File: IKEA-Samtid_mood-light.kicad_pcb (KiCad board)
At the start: 2 copper layers, 100 x 100 mm, 156 parts, among them IC1 ATMEGA168PA-M, P1 FTDI, P2 POWER, P3.1 B-to-B-1A, P3.2 B-to-B-1B, P4.1 B-to-B-2A, P4.2 B-to-B-2B, Q1 BSS138, Q2 BSS138, SW1 ENTER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

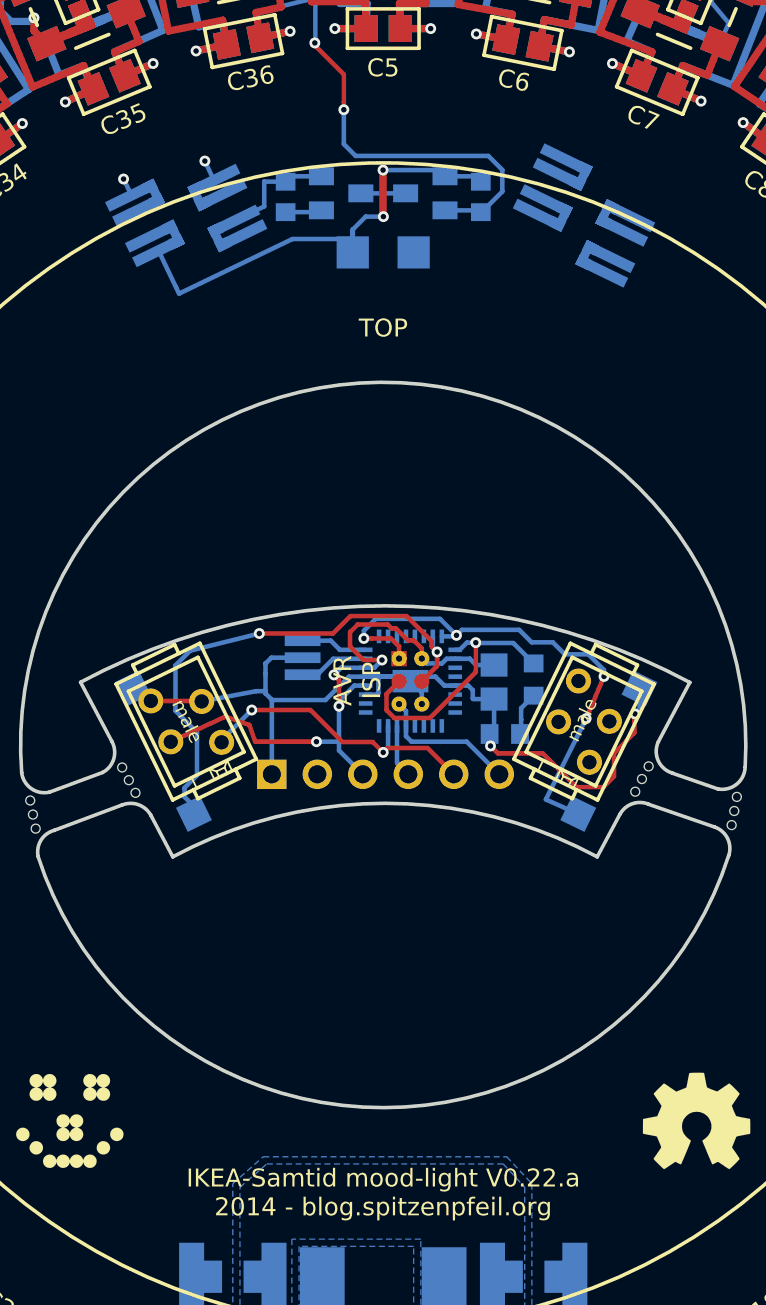
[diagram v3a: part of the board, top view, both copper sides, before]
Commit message: Had the pull-up voltages reversed on the MOSFET isolator.
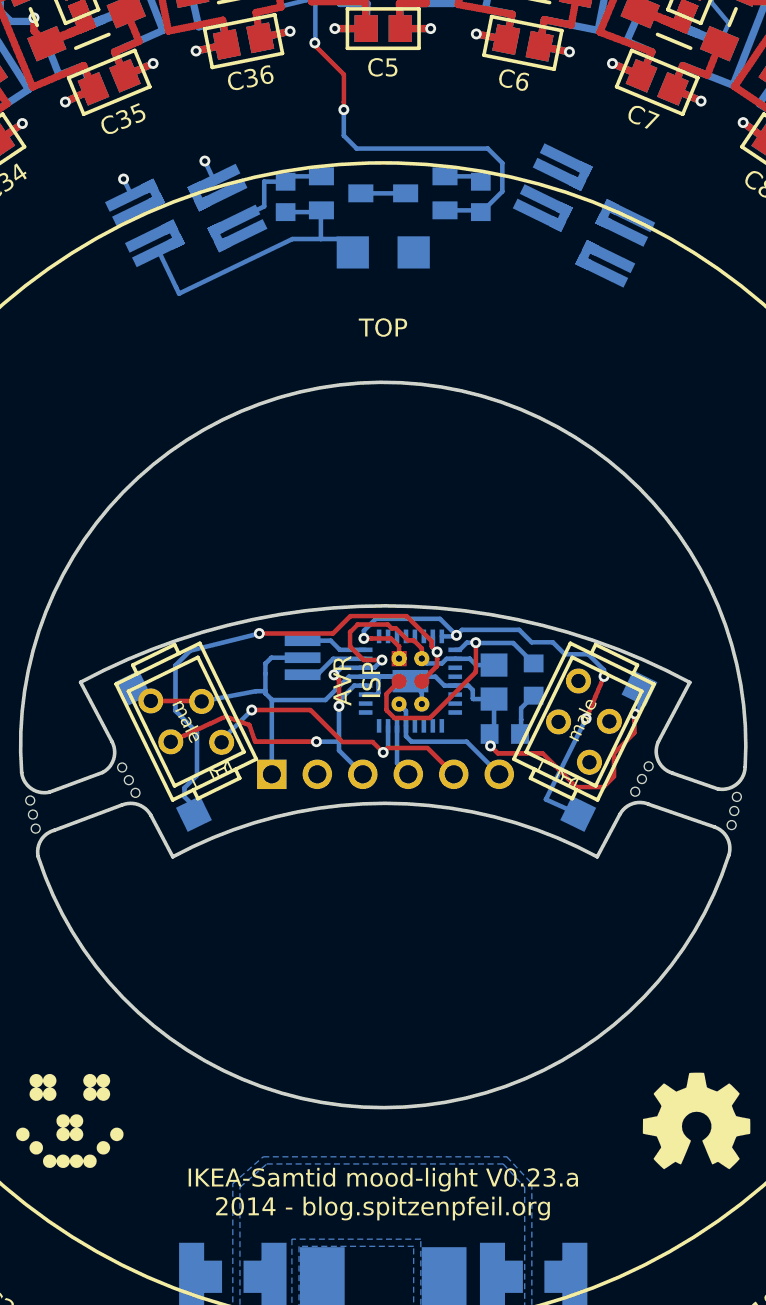
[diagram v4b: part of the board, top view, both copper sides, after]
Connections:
- Q1 pad 1: /VCC.A -> +5V
- Q2 pad 1: +5V -> /VCC.A
- Rp1 pad 1: +5V -> /VCC.A
- Rp2 pad 1: /VCC.A -> +5V
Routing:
- net /VCC.A: track 25.3 -> 16.6 mm, vias 2 -> 0
- net +5V: track 626.2 -> 627.0 mm
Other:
- board text added: "IKEA-Samtid mood-light V0.23.a 2014 - blog.spitzenpfeil.org"
- board text removed: "IKEA-Samtid mood-light V0.22.a 2014 - blog.spitzenpfeil.org"
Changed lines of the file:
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@@
     (thickness 1.6)
     (drawings 55)
-    (tracks 1446)
+    (tracks 1438)
     (zones 0)
     (modules 156)
@@
     (title IKEA-Samtid_mood-light)
     (date "25 Jul 2014")
-    (rev 0.22.a)
+    (rev 0.23.a)
     (company "2014 - blog.spitzenpfeil.org")
   )
@@
     (add_net "Net-(D65-Pad2)")
     (add_net "Net-(DS1-Pad2)")
+    (add_net "Net-(IC1-Pad28)")
     (add_net "Net-(LED1-Pad2)")
     (add_net "Net-(LED10-Pad2)")
@@
     (add_net "Net-(P4.1-Pad3)")
     (add_net "Net-(P4.1-Pad4)")
+    (add_net "Net-(P4.2-Pad2)")
     (add_net "Net-(Q1-Pad3)")
   )
@@
     (fp_line (start -1.41986 0.65786) (end 1.41986 0.65786) (layer B.SilkS) (width 0.2))
     (pad 1 smd rect (at -0.95 -1.1 270) (size 1 1.4) (layers B.Cu B.Paste B.Mask)
-      (net 76 /VCC.A))
+      (net 1 +5V))
     (pad 2 smd rect (at 0.95 -1.1 270) (size 1 1.4) (layers B.Cu B.Paste B.Mask)
       (net 4 /WS2812B-LEDs-1/A_IN))
@@
     (fp_line (start -1.41986 0.65786) (end 1.41986 0.65786) (layer B.SilkS) (width 0.2))
     (pad 1 smd rect (at -0.95 -1.1 90) (size 1 1.4) (layers B.Cu B.Paste B.Mask)
-      (net 1 +5V))
+      (net 76 /VCC.A))
     (pad 2 smd rect (at 0.95 -1.1 90) (size 1 1.4) (layers B.Cu B.Paste B.Mask)
       (net 79 /TXO/LEDs))
@@
     (fp_line (start 0.4318 0.3556) (end -0.4318 0.3556) (layer B.SilkS) (width 0.2))
     (pad 1 smd rect (at -0.84836 0 90) (size 0.99822 1.09982) (layers B.Cu B.Paste B.Mask)
-      (net 1 +5V))
+      (net 76 /VCC.A))
     (pad 2 smd rect (at 0.84836 0 90) (size 0.99822 1.09982) (layers B.Cu B.Paste B.Mask)
       (net 79 /TXO/LEDs))
@@
     (fp_line (start 0.4318 0.3556) (end -0.4318 0.3556) (layer B.SilkS) (width 0.2))
     (pad 1 smd rect (at -0.84836 0 270) (size 0.99822 1.09982) (layers B.Cu B.Paste B.Mask)
-      (net 76 /VCC.A))
+      (net 1 +5V))
     (pad 2 smd rect (at 0.84836 0 270) (size 0.99822 1.09982) (layers B.Cu B.Paste B.Mask)
       (net 4 /WS2812B-LEDs-1/A_IN))
@@
     (effects (font (size 0.75 0.75) (thickness 0.1875)) (justify mirror))
   )
-  (gr_text "IKEA-Samtid mood-light V0.22.a\n2014 - blog.spitzenpfeil.org" (at 150 120) (layer F.SilkS)
+  (gr_text "IKEA-Samtid mood-light V0.23.a\n2014 - blog.spitzenpfeil.org" (at 150 120) (layer F.SilkS)
     (effects (font (size 1 1) (thickness 0.2)))
   )
@@
   )
   (gr_circle (center 150 95) (end 170.25 95) (layer Eco1.User) (width 0.2))
+  (segment (start 153.1 62.9) (end 153.45 63.25) (width 0.254) (layer B.Cu) (net 1))
+  (segment (start 155.14836 63.25) (end 155.45 63.55164) (width 0.254) (layer B.Cu) (net 1) (status 30))
+  (segment (start 153.45 63.25) (end 155.14836 63.25) (width 0.254) (layer B.Cu) (net 1) (status 30))
   (segment (start 164.424267 132.268124) (end 162.85 133) (width 0.4064) (layer B.Cu) (net 1) (status 10))
   (segment (start 162.85 133) (end 164.424267 132.268124) (width 0.4064) (layer F.Cu) (net 1) (status 20))
@@
   (segment (start 144.8 55.15) (end 143.131545 55.513859) (width 0.4064) (layer F.Cu) (net 1) (status 20))
   (segment (start 143.131545 55.513859) (end 144.8 55.15) (width 0.4064) (layer B.Cu) (net 1) (status 10))
-  (segment (start 144.55 65.24836) (end 146.45164 65.24836) (width 0.254) (layer B.Cu) (net 1) (status 30))
   (segment (start 147.07 89.18) (end 147.57994 89.68994) (width 0.254) (layer B.Cu) (net 2))
   (segment (start 147.57994 89.68994) (end 149.02064 89.68994) (width 0.254) (layer B.Cu) (net 2))
@@
   (segment (start 145.5 91.08) (end 146.32 91.08) (width 0.254) (layer B.Cu) (net 3))
   (segment (start 155.45 65.24836) (end 155.5008 65.24836) (width 0.254) (layer B.Cu) (net 4))
-  (segment (start 148.46 62.11) (end 147.8 61.45) (width 0.254) (layer B.Cu) (net 4))
+  (segment (start 148.52 61.7) (end 147.8 60.98) (width 0.254) (layer B.Cu) (net 4))
   (segment (start 155.5008 65.24836) (end 156.65 64.09916) (width 0.254) (layer B.Cu) (net 4))
-  (segment (start 156.65 64.09916) (end 156.65 62.89) (width 0.254) (layer B.Cu) (net 4))
-  (segment (start 156.65 62.89) (end 155.87 62.11) (width 0.254) (layer B.Cu) (net 4))
-  (segment (start 155.87 62.11) (end 148.46 62.11) (width 0.254) (layer B.Cu) (net 4))
-  (segment (start 147.8 61.45) (end 147.8 59.53) (width 0.254) (layer B.Cu) (net 4))
+  (segment (start 156.65 64.09916) (end 156.65 62.51) (width 0.254) (layer B.Cu) (net 4))
+  (segment (start 156.65 62.51) (end 155.84 61.7) (width 0.254) (layer B.Cu) (net 4))
+  (segment (start 155.84 61.7) (end 148.52 61.7) (width 0.254) (layer B.Cu) (net 4))
+  (segment (start 147.8 60.98) (end 147.8 59.53) (width 0.254) (layer B.Cu) (net 4))
   (segment (start 147.8 59.098948) (end 147.8 59.53) (width 0.254) (layer F.Cu) (net 4))
   (segment (start 146.18 55.94) (end 147.8 57.56) (width 0.254) (layer F.Cu) (net 4))
@@
   (segment (start 142.52067 93.88602) (end 142.855187 94.822667) (width 0.254) (layer F.Cu) (net 75))
   (segment (start 138.136897 94.827466) (end 141.19479 93.41739) (width 0.254) (layer F.Cu) (net 75))
-  (segment (start 149.99 62.9) (end 153.1 62.9) (width 0.254) (layer B.Cu) (net 76))
-  (segment (start 153.1 62.9) (end 153.45 63.25) (width 0.254) (layer B.Cu) (net 76))
-  (segment (start 150.01 65.5) (end 149.99 65.48) (width 0.254) (layer F.Cu) (net 76))
-  (via (at 150.01 65.5) (size 0.6096) (layers F.Cu B.Cu) (net 76))
-  (segment (start 150.01 65.5) (end 150 65.5) (width 0.254) (layer B.Cu) (net 76))
-  (segment (start 149.99 62.9) (end 150.03 62.9) (width 0.254) (layer B.Cu) (net 76))
-  (via (at 149.99 62.9) (size 0.6096) (layers F.Cu B.Cu) (net 76))
-  (segment (start 149.99 65.48) (end 149.99 62.9) (width 0.4064) (layer F.Cu) (net 76))
-  (segment (start 155.14836 63.25) (end 155.45 63.55164) (width 0.254) (layer B.Cu) (net 76) (status 30))
-  (segment (start 153.45 63.25) (end 155.14836 63.25) (width 0.254) (layer B.Cu) (net 76) (status 30))
-  (segment (start 150.01 65.5) (end 149.02 65.5) (width 0.254) (layer B.Cu) (net 76))
-  (segment (start 148.3 66.22) (end 148.3 67.5) (width 0.254) (layer B.Cu) (net 76))
-  (segment (start 149.02 65.5) (end 148.3 66.22) (width 0.254) (layer B.Cu) (net 76))
-  (segment (start 144.931379 66.75) (end 148.3 66.75) (width 0.254) (layer B.Cu) (net 76))
+  (segment (start 146.52 66.75) (end 148.3 66.75) (width 0.254) (layer B.Cu) (net 76))
+  (segment (start 144.931379 66.75) (end 146.52 66.75) (width 0.254) (layer B.Cu) (net 76))
   (segment (start 138.6 69.8) (end 144.931379 66.75) (width 0.254) (layer B.Cu) (net 76))
   (segment (start 138.430306 69.44583) (end 138.6 69.8) (width 0.254) (layer B.Cu) (net 76))
-  (segment (start 148.3 66.75) (end 148.3 66.22) (width 0.254) (layer B.Cu) (net 76))
   (segment (start 137.451154 67.397033) (end 138.430306 69.44583) (width 0.254) (layer B.Cu) (net 76))
+  (segment (start 144.55 65.24836) (end 146.45164 65.24836) (width 0.254) (layer B.Cu) (net 76) (status 30))
+  (segment (start 146.52 65.18) (end 146.55 65.15) (width 0.254) (layer B.Cu) (net 76))
+  (segment (start 146.52 66.75) (end 146.52 65.18) (width 0.254) (layer B.Cu) (net 76))
   (segment (start 135.943157 64.305181) (end 135.5 63.4) (width 0.254) (layer B.Cu) (net 77))
   (via (at 135.5 63.4) (size 0.6096) (layers F.Cu B.Cu) (net 77))

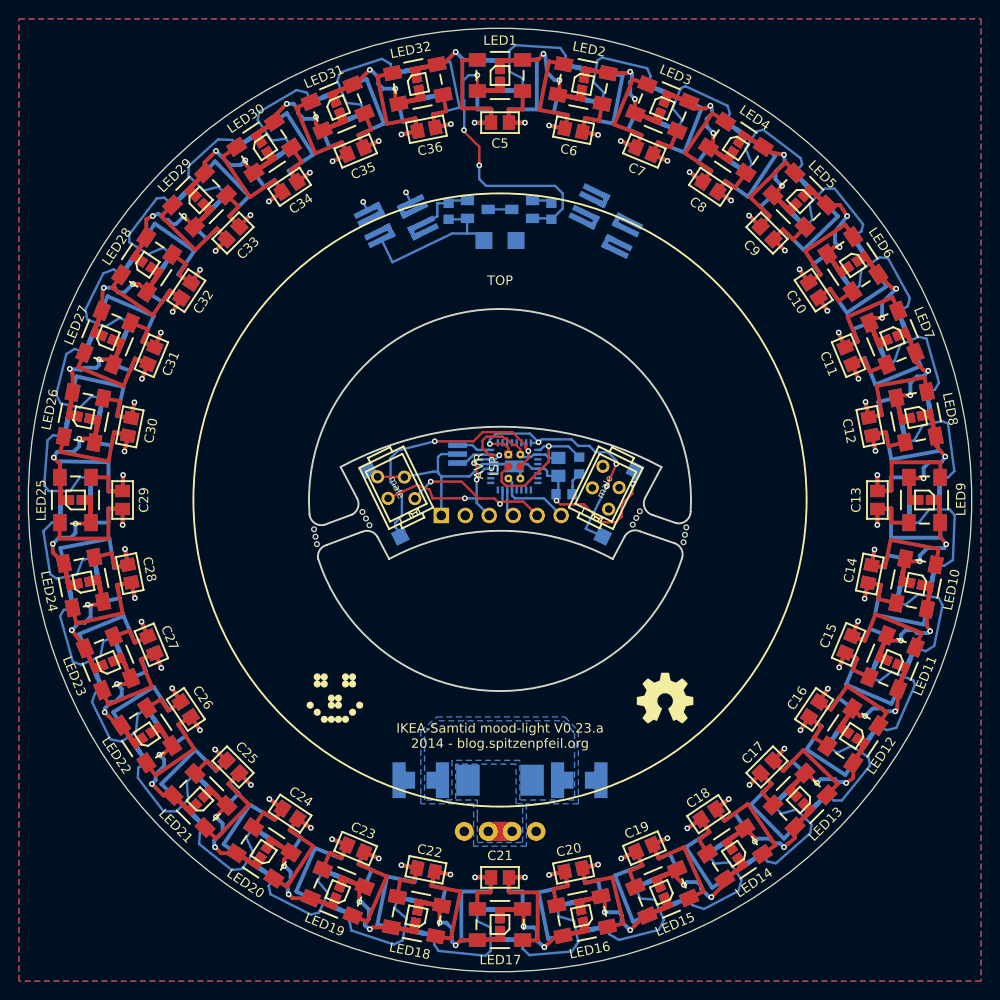
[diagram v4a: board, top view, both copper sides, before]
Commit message: Massive silkscreen cleanup + tweaks. Power-connector larger holes.
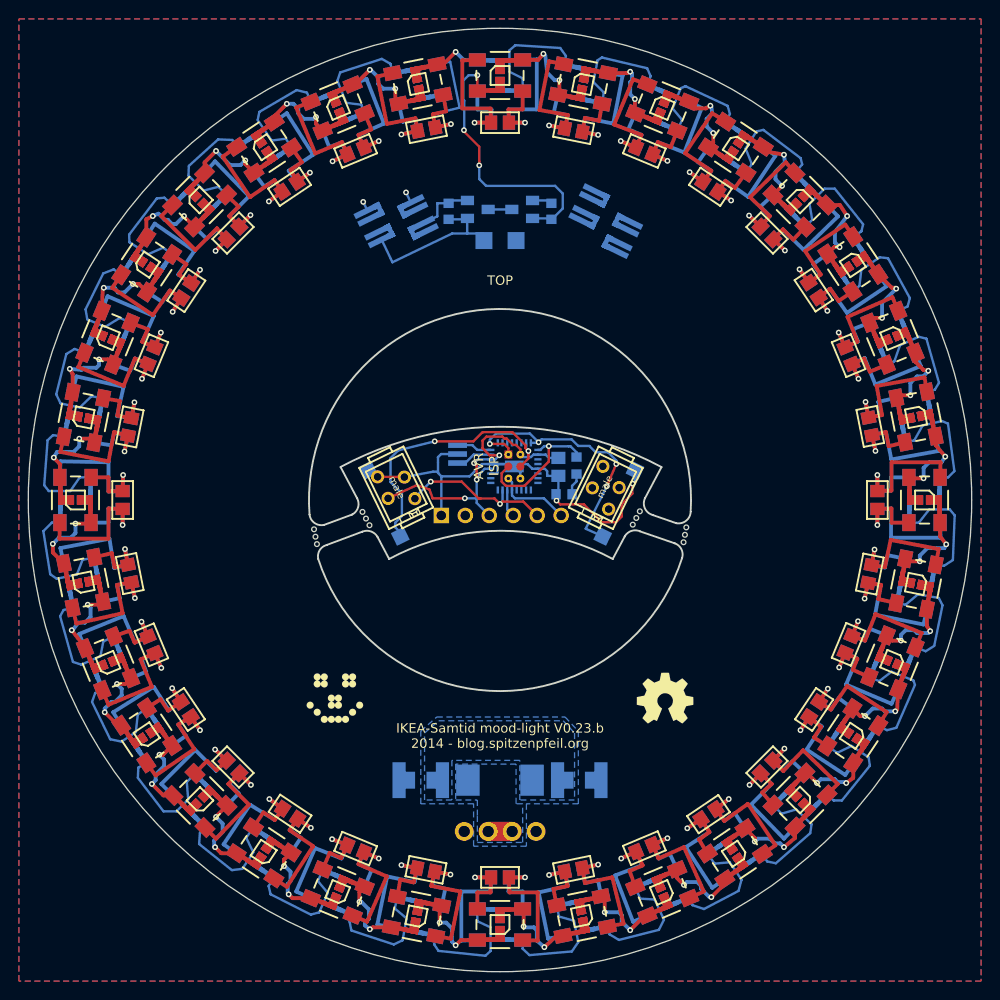
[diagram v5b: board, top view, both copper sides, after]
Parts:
- moved D65 0.29 mm to (158.1, 91.3)
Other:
- board text added: "5V-4A"
- board text added: "IKEA-Samtid mood-light V0.23.b 2014 - blog.spitzenpfeil.org"
- board text removed: "5V"
- board text removed: "IKEA-Samtid mood-light V0.23.a 2014 - blog.spitzenpfeil.org"

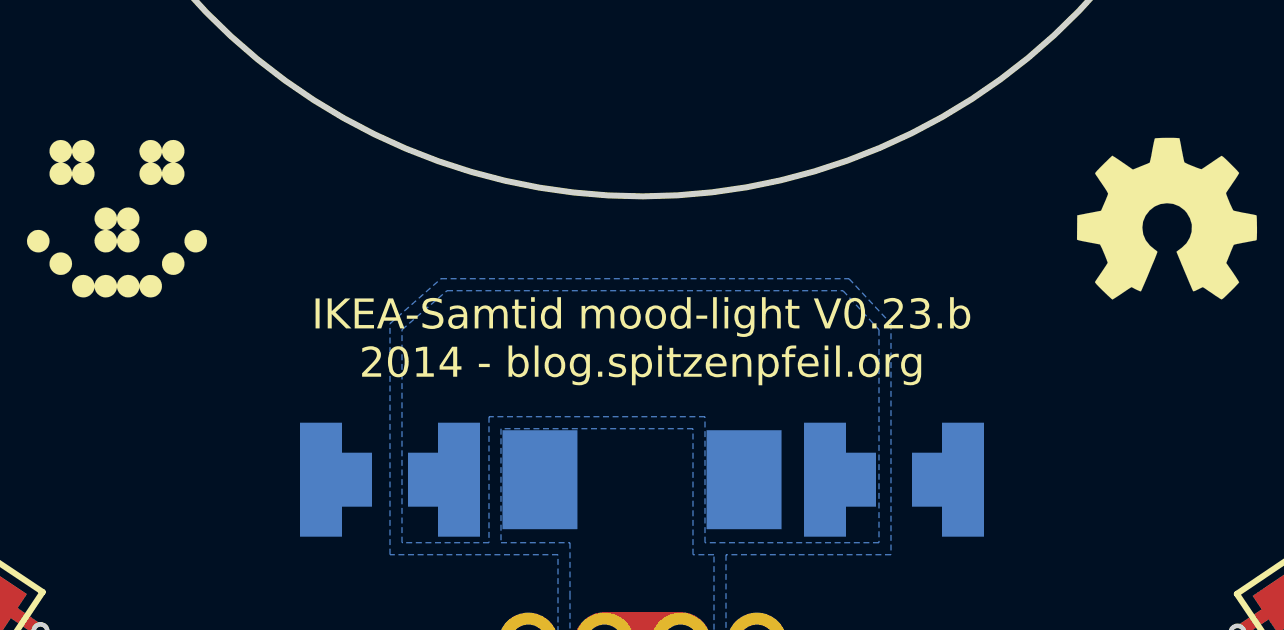
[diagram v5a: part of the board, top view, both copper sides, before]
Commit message: Changed pull-up resistors to 1.5k. Roughly following: (VCC-0.4)/0.003
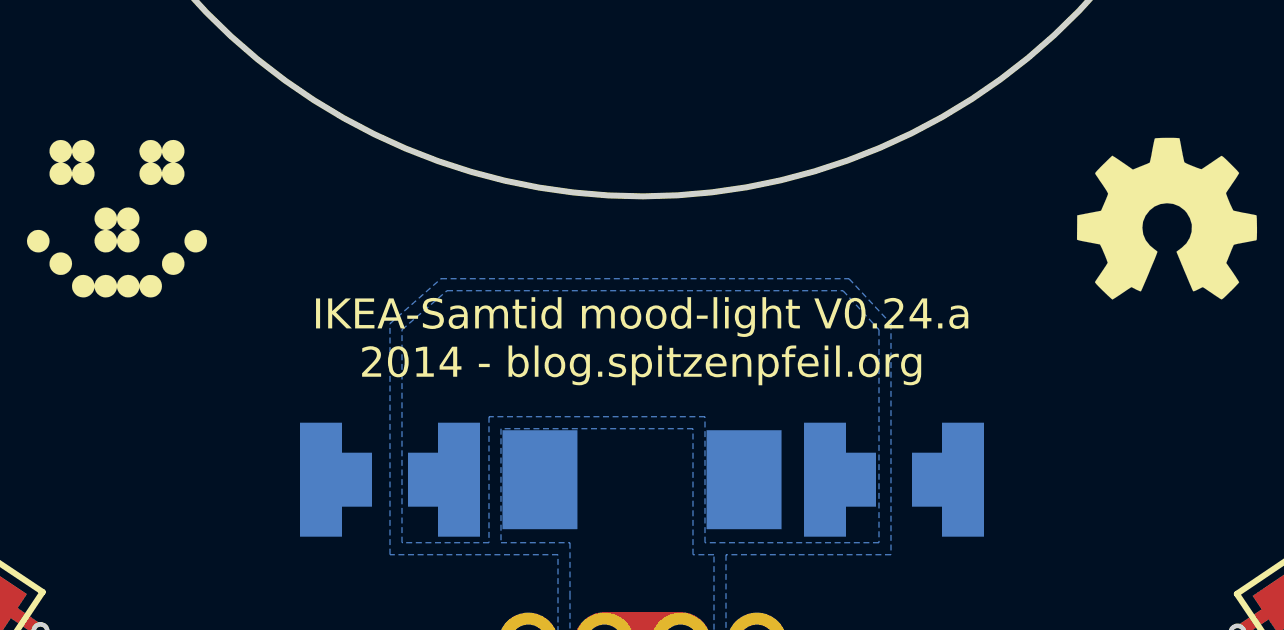
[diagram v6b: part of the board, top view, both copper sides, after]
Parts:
- Rp1, Rp2: value 4k7 -> 1k5
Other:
- board text added: "IKEA-Samtid mood-light V0.24.a 2014 - blog.spitzenpfeil.org"
- board text removed: "IKEA-Samtid mood-light V0.23.b 2014 - blog.spitzenpfeil.org"
